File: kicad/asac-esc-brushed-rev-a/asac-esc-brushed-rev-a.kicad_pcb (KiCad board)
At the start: 2 copper layers, 49.7 x 49.8 mm, 21 parts, among them J1 M1, J14 Conn_01x03, J2 Battery, J3 FC Connector, Q1 AO3480C, U1 HT7533S, U2 INA180A4, U3 STM32C011F6Px

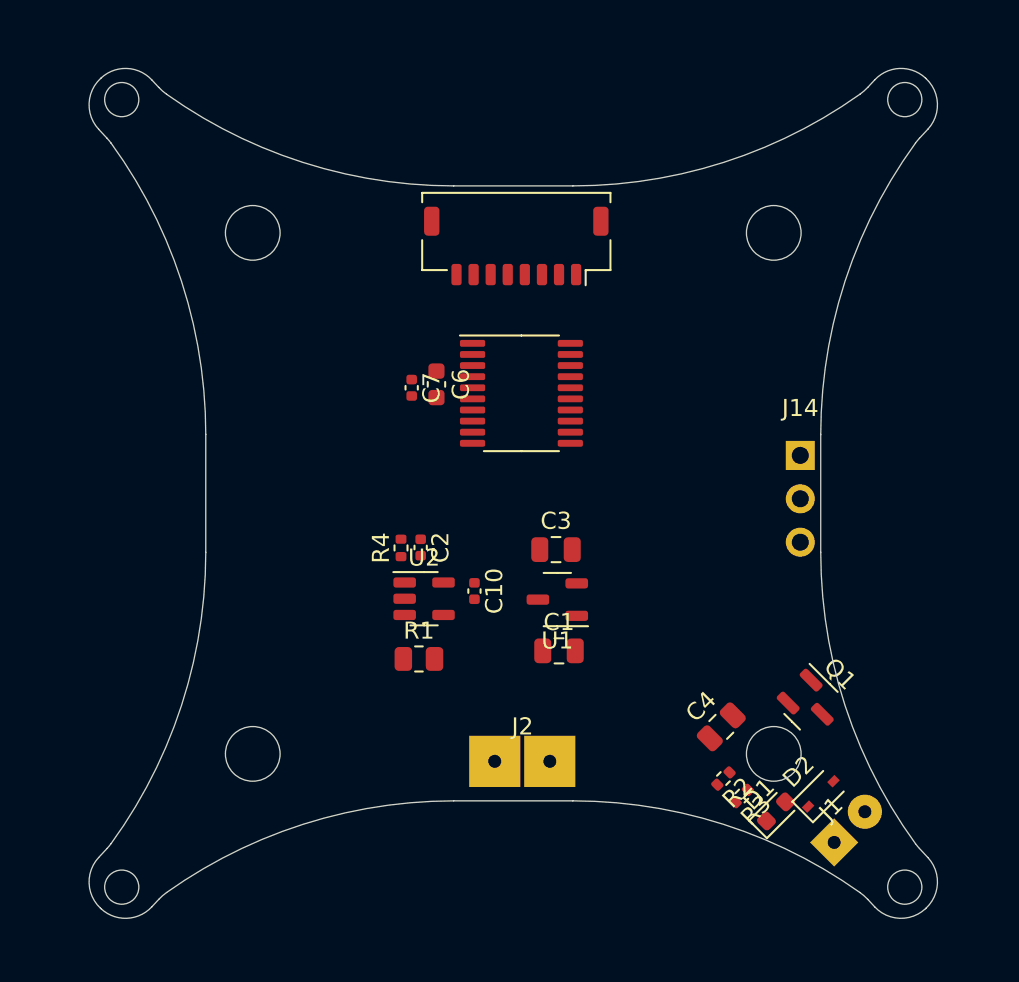
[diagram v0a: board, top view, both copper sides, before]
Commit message: Finished rev A schematic, layout and routing
All that is left now is to add some graphics!
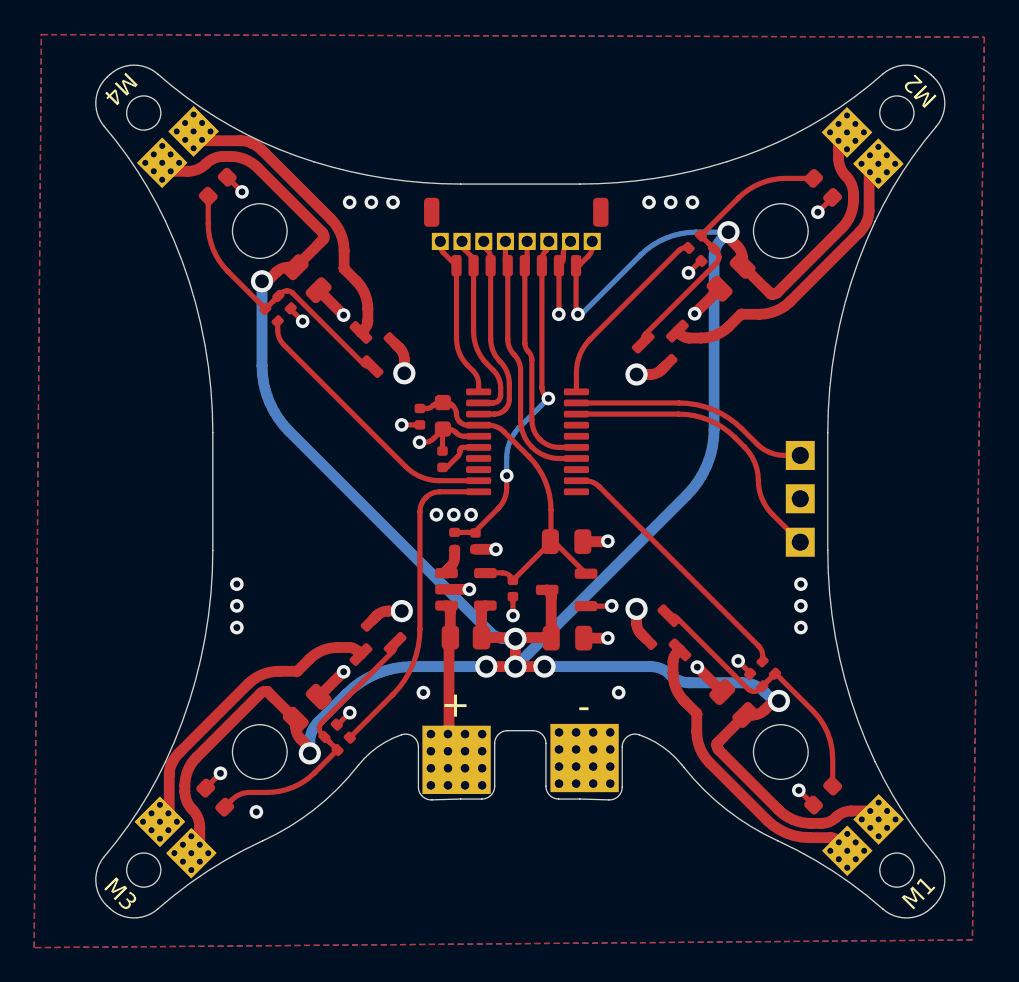
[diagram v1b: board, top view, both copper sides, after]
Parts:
- added C11: 100n, Capacitor_SMD:C_0402_1005Metric, F.Cu at (141.6, 98.9)
- added C5: 10u, Capacitor_SMD:C_0805_2012Metric, F.Cu at (158.5, 88.2)
- added C8: 10u, Capacitor_SMD:C_0805_2012Metric, F.Cu at (133.7, 113.4)
- added C9: 10u, Capacitor_SMD:C_0805_2012Metric, F.Cu at (133.7, 88.3)
- added D3: RED, LED_SMD:LED_0603_1608Metric, F.Cu at (163.9, 83.0)
- added D4: SD103AWS, Diode_SMD:D_SOD-323, F.Cu at (159.8, 89.6)
- added D5: RED, LED_SMD:LED_0603_1608Metric, F.Cu at (128.3, 118.7)
- added D6: SD103AWS, Diode_SMD:D_SOD-323, F.Cu at (132.3, 112.0)
- added D7: RED, LED_SMD:LED_0603_1608Metric, F.Cu at (128.4, 82.9)
- added D8: SD103AWS, Diode_SMD:D_SOD-323, F.Cu at (135.1, 87.0)
- added J4: M2, Custom:Conn_01x02_VBAT_one_round, F.Cu at (166.2, 80.6)
- added J5: M3, Custom:Conn_01x02_VBAT_one_round, F.Cu at (126.0, 121.0)
- added J6: M4, Custom:Conn_01x02_VBAT_one_round, F.Cu at (126.1, 80.6)
- added J7: FC 1.27mm Pin Connector, Connector_PinHeader_1.27mm:PinHeader_1x08_P1.27mm_Vertical, F.Cu at (150.3, 86.1)
- added Q2: AO3480C, Package_TO_SOT_SMD:SOT-23, F.Cu at (154.7, 92.0)
- added Q3: AO3480C, Package_TO_SOT_SMD:SOT-23, F.Cu at (137.5, 109.6)
- added Q4: AO3480C, Package_TO_SOT_SMD:SOT-23, F.Cu at (137.5, 92.1)
- added R10: 10k, Resistor_SMD:R_0402_1005Metric, F.Cu at (132.3, 89.7)
- added R5: 470R, Resistor_SMD:R_0402_1005Metric, F.Cu at (156.3, 86.1)
- added R6: 10k, Resistor_SMD:R_0402_1005Metric, F.Cu at (157.1, 86.9)
- added R7: 470R, Resistor_SMD:R_0402_1005Metric, F.Cu at (135.8, 115.5)
- added R8: 10k, Resistor_SMD:R_0402_1005Metric, F.Cu at (135.0, 114.8)
- added R9: 470R, Resistor_SMD:R_0402_1005Metric, F.Cu at (131.6, 90.4)
- J14: value Conn_01x03 -> SWD Debug
- J3: value FC Connector -> FC JST 1.0mm Connector
- U2: value INA180A4 -> INA180A4IDBVR
- moved Q1 9.15 mm to (154.8, 109.4)
- moved D2 7.63 mm to (157.2, 114.5), turned to 135 degrees
- moved R2 7.02 mm to (160.7, 111.0), turned to 135 degrees
- moved R3 6.84 mm to (159.9, 111.8), turned to 135 degrees
- moved C2 3.23 mm to (143.5, 103.7)
- moved R4 3.17 mm to (142.3, 103.7)
- moved R1 3.02 mm to (143.0, 109.3)
- moved J1 2.93 mm to (166.2, 120.9), turned to -135 degrees
- moved D1 2.91 mm to (163.9, 118.5)
- moved U3 2.86 mm to (146.6, 97.8)
- moved U2 2.51 mm to (143.0, 106.5)
- moved J2 2.39 mm to (145.8, 116.3), turned to 180 degrees
- moved C10 2.26 mm to (145.7, 106.4)
- moved C6 1.88 mm to (141.6, 96.3)
- moved C7 1.76 mm to (140.3, 96.4)
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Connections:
- U3 pad 1: unconnected-(U3-Pad1) -> SIGNAL_M4
- U3 pad 10: unconnected-(U3-Pad10) -> M3
- U3 pad 12: unconnected-(U3-Pad12) -> M1
- U3 pad 14: unconnected-(U3-Pad14) -> SIGNAL_M1
- U3 pad 15: unconnected-(U3-Pad15) -> Telemetry
- U3 pad 2: unconnected-(U3-Pad2) -> SIGNAL_M3
- U3 pad 20: unconnected-(U3-Pad20) -> M2
- U3 pad 3: unconnected-(U3-Pad3) -> SIGNAL_M2
- U3 pad 6: unconnected-(U3-Pad6) -> Net-(U3-Pad6)
- U3 pad 9: unconnected-(U3-Pad9) -> M4
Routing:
- net VCC: track 0.00 -> 178.1 mm, vias 0 -> 9
- net GND: track 0.00 -> 44.3 mm, vias 0 -> 43
- net +3.3V: track 0.00 -> 21.1 mm
- net Current: track 0.00 -> 20.1 mm, vias 0 -> 2
- net M3: track 0.00 -> 18.8 mm
- net SWDIO: track 0.00 -> 17.1 mm
- net Net-(D6-Pad2): track 0.00 -> 16.8 mm
- net Net-(D8-Pad2): track 0.00 -> 16.8 mm
- net Net-(D4-Pad2): track 0.00 -> 16.8 mm
- net Net-(D2-Pad2): track 0.00 -> 16.7 mm
- net Net-(D3-Pad2): track 0.00 -> 16.3 mm
- net Net-(D7-Pad2): track 0.00 -> 16.3 mm
- net Net-(D1-Pad2): track 0.00 -> 16.2 mm
- net Net-(D5-Pad2): track 0.00 -> 16.2 mm
- net M4: track 0.00 -> 16.0 mm
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- added copper zone on B.Cu, net GND
- added copper zone on F.Cu, net GND
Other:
- board size 49.7 x 49.8 mm -> 49.7 x 49.9 mm
- board text added: "+"
- board text added: "-"
- board text added: "CURR"
- board text added: "GND"
- board text added: "M1"
- board text added: "M2"
- board text added: "M3"
- board text added: "M4"
- board text added: "TELEM"
- board text added: "VBAT"

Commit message: Rev. A ready for order!
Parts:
- J14: footprint Custom:PinSocket_1x03_P2.54mm_Vertical_No_silk -> Connector_PinHeader_1.27mm:PinHeader_1x03_P1.27mm_Vertical
- moved J14 0.92 mm to (163.4, 98.6)
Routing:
- net SWDIO: track 17.1 -> 15.6 mm
- net SWCLK: track 14.0 -> 14.9 mm
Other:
- board text added: "SWC"
- board text added: "SWD"
- board text removed: "+"
- board text removed: "-"
